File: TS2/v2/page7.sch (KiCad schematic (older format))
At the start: 9 parts, among them P1 FTDI (TERMINAL), P2 FTDI (HOST), U29 6850, U3 74LS00, U30 6850, U31 MC14411, U5 74LS04, Y1 1.842MHz

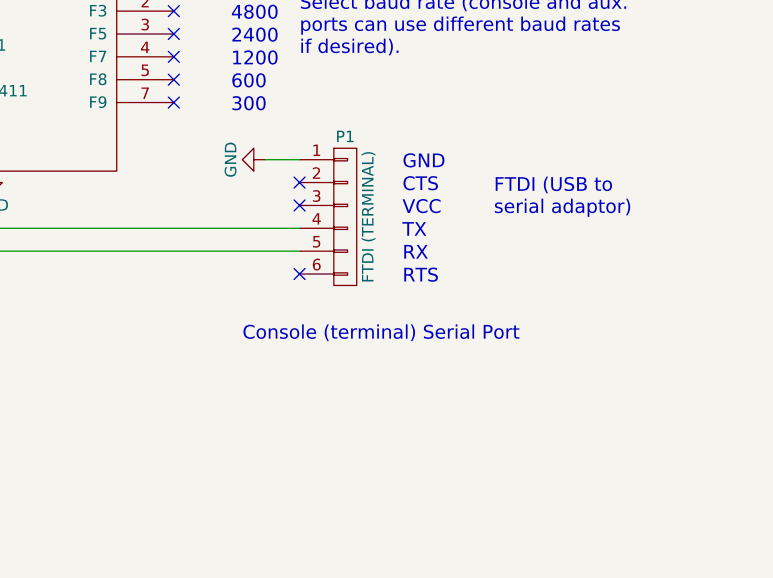
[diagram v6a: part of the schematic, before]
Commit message: Add note about powering from USB.
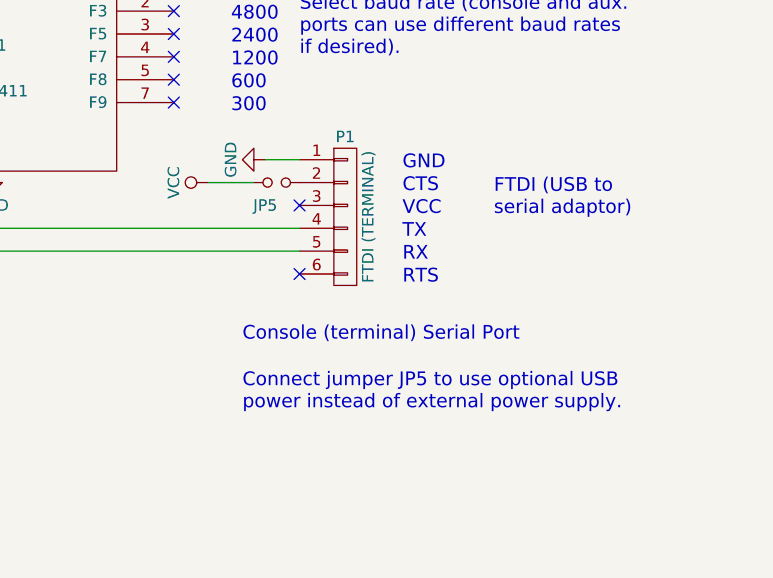
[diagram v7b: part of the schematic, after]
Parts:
- added JP5: Jumper_NO_Small, symbol Jumper_NO_Small
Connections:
- net VCC: now also JP5.1
- net at P1.2 (P2): now also JP5.2
- no-connect marks 13 -> 12
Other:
- note added: "Connect jumper JP5 to use optional USB\npower instead of external power supply."
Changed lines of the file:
@@
 RTS
 NoConn ~ 8600 2500
-NoConn ~ 8600 2100
 NoConn ~ 8600 5350
 NoConn ~ 8600 4950
@@
 Text Notes 8450 4550 0    60   ~ 0
 Auxiliary (host) Serial Port
+NoConn ~ 8600 2200
+NoConn ~ 8600 5050
+Wire Wire Line
+	5300 800  5300 1850
+Wire Wire Line
+	5100 4700 5100 600
+Wire Wire Line
+	5100 600  8200 600
+Wire Wire Line
+	8200 600  8200 1250
+Connection ~ 8050 1250
+$Comp
+L Jumper_NO_Small JP5
+U 1 1 586F01C1
+P 8500 2100
+F 0 "JP5" H 8450 2000 50  0000 C CNN
+F 1 "Jumper_NO_Small" H 8510 2040 50  0001 C CNN
+F 2 "" H 8500 2100 50  0000 C CNN
+F 3 "" H 8500 2100 50  0000 C CNN
+	1    8500 2100
+	1    0    0    -1
+$EndComp
+$Comp
+L VCC #PWR0101
+U 1 1 586F01FE
+P 8200 2100
+F 0 "#PWR0101" H 8200 1950 50  0001 C CNN
+F 1 "VCC" H 8200 2250 50  0000 C CNN
+F 2 "" H 8200 2100 50  0000 C CNN
+F 3 "" H 8200 2100 50  0000 C CNN
+	1    8200 2100
+	0    -1   -1   0
+$EndComp
+Wire Wire Line
+	8200 2100 8400 2100
 Text Notes 8350 2800 0    60   ~ 0
 Console (terminal) Serial Port
-NoConn ~ 8600 2200
-NoConn ~ 8600 5050
-Wire Wire Line
-	5300 800  5300 1850
-Wire Wire Line
-	5100 4700 5100 600
-Wire Wire Line
-	5100 600  8200 600
-Wire Wire Line
-	8200 600  8200 1250
-Connection ~ 8050 1250
+Text Notes 8350 3100 0    60   ~ 0
+Connect jumper JP5 to use optional USB\npower instead of external power supply.
 $EndSCHEMATC
